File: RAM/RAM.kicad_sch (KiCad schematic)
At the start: 32 parts, among them J1 Conn_01x02_Pin, J2 Conn_01x02_Pin, J3 Conn_01x04_Pin, J4 Conn_01x04_Pin, J5 Conn_01x08_Socket, U2 CD74HCT258E, U3 SN74HCT245N, U4 CD74HCT258E, U6 CD74HCT258E

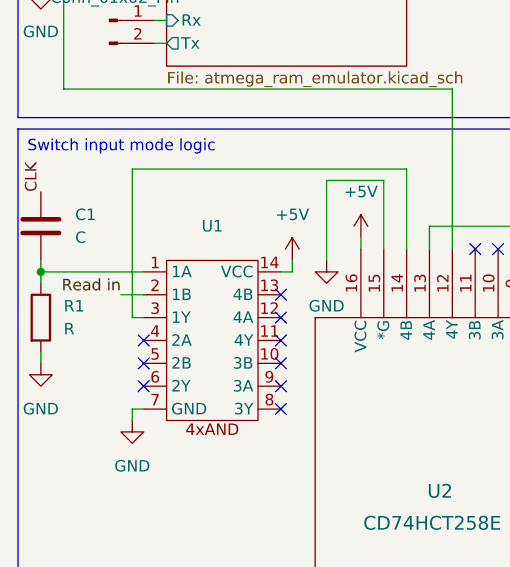
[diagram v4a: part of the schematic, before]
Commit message: Assigned footprints to all RAM components except crystal. No datasheet so waiting for delivery to hopefully get more detail or measure
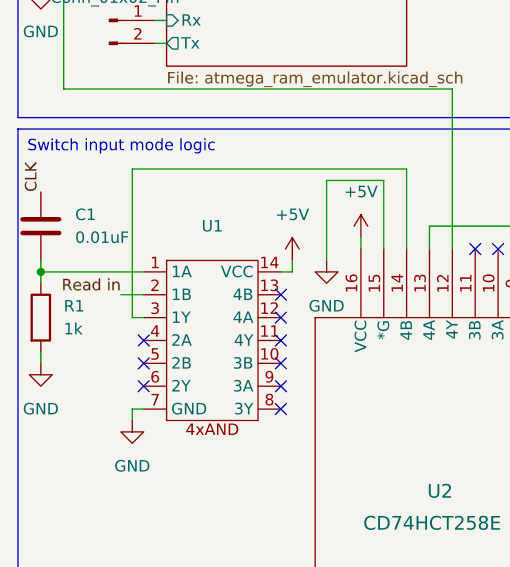
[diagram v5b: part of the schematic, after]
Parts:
- C1: value C -> 0.01uF; footprint (none) -> Capacitor_THT:C_Disc_D5.0mm_W2.5mm_P2.50mm
- J1, J2: footprint (none) -> Connector_PinHeader_1.00mm:PinHeader_1x02_P1.00mm_Vertical
- J3, J4: footprint (none) -> Connector_PinHeader_1.00mm:PinHeader_1x04_P1.00mm_Horizontal
- R1: value R -> 1k; footprint (none) -> _DownloadFootprints:CF_series_Resistors_THT
- U1: footprint (none) -> 8BitCPUFootprints:4x_and
- U2, U4, U6: footprint N16 -> _DownloadFootprints:2_to_1_selector
- U5: footprint (none) -> Package_DIP:DIP-16_W7.62mm
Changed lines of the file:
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@@
 			)
 		)
-		(property "Footprint" ""
+		(property "Footprint" "Package_DIP:DIP-16_W7.62mm"
 			(at 203.2 146.05 0)
 			(effects
@@
 			)
 		)
-		(property "Footprint" "N16"
+		(property "Footprint" "_DownloadFootprints:2_to_1_selector"
 			(at 184.15 88.9 0)
 			(effects
@@
 			)
 		)
-		(property "Footprint" ""
+		(property "Footprint" "Connector_PinHeader_1.00mm:PinHeader_1x02_P1.00mm_Vertical"
 			(at 30.48 100.33 0)
 			(effects
@@
 			)
 		)
-		(property "Footprint" ""
+		(property "Footprint" "Connector_PinHeader_1.00mm:PinHeader_1x02_P1.00mm_Vertical"
 			(at 30.48 60.96 0)
 			(effects
@@
 			)
 		)
-		(property "Footprint" "N16"
+		(property "Footprint" "_DownloadFootprints:2_to_1_selector"
 			(at 214.63 88.9 0)
 			(effects
@@
 			)
 		)
-		(property "Value" "R"
+		(property "Value" "1k"
 			(at 25.4 134.6199 0)
 			(effects
@@
 			)
 		)
-		(property "Footprint" ""
+		(property "Footprint" "_DownloadFootprints:CF_series_Resistors_THT"
 			(at 21.082 133.35 90)
 			(effects
@@
 			)
 		)
-		(property "Footprint" ""
+		(property "Footprint" "Connector_PinHeader_1.00mm:PinHeader_1x04_P1.00mm_Horizontal"
 			(at 266.7 38.1 0)
 			(effects
@@
 			)
 		)
-		(property "Footprint" "N16"
+		(property "Footprint" "_DownloadFootprints:2_to_1_selector"
 			(at 58.42 181.61 0)
 			(effects
@@
 			)
 		)
-		(property "Value" "C"
+		(property "Value" "0.01uF"
 			(at 26.67 124.4599 0)
 			(effects
@@
 			)
 		)
-		(property "Footprint" ""
+		(property "Footprint" "Capacitor_THT:C_Disc_D5.0mm_W2.5mm_P2.50mm"
 			(at 23.8252 127 0)
 			(effects
@@
 			)
 		)
-		(property "Footprint" ""
+		(property "Footprint" "Connector_PinHeader_1.00mm:PinHeader_1x04_P1.00mm_Horizontal"
 			(at 49.53 20.32 0)
 			(effects
@@
 			)
 		)
-		(property "Footprint" ""
+		(property "Footprint" "8BitCPUFootprints:4x_and"
 			(at 36.83 133.35 0)
 			(effects

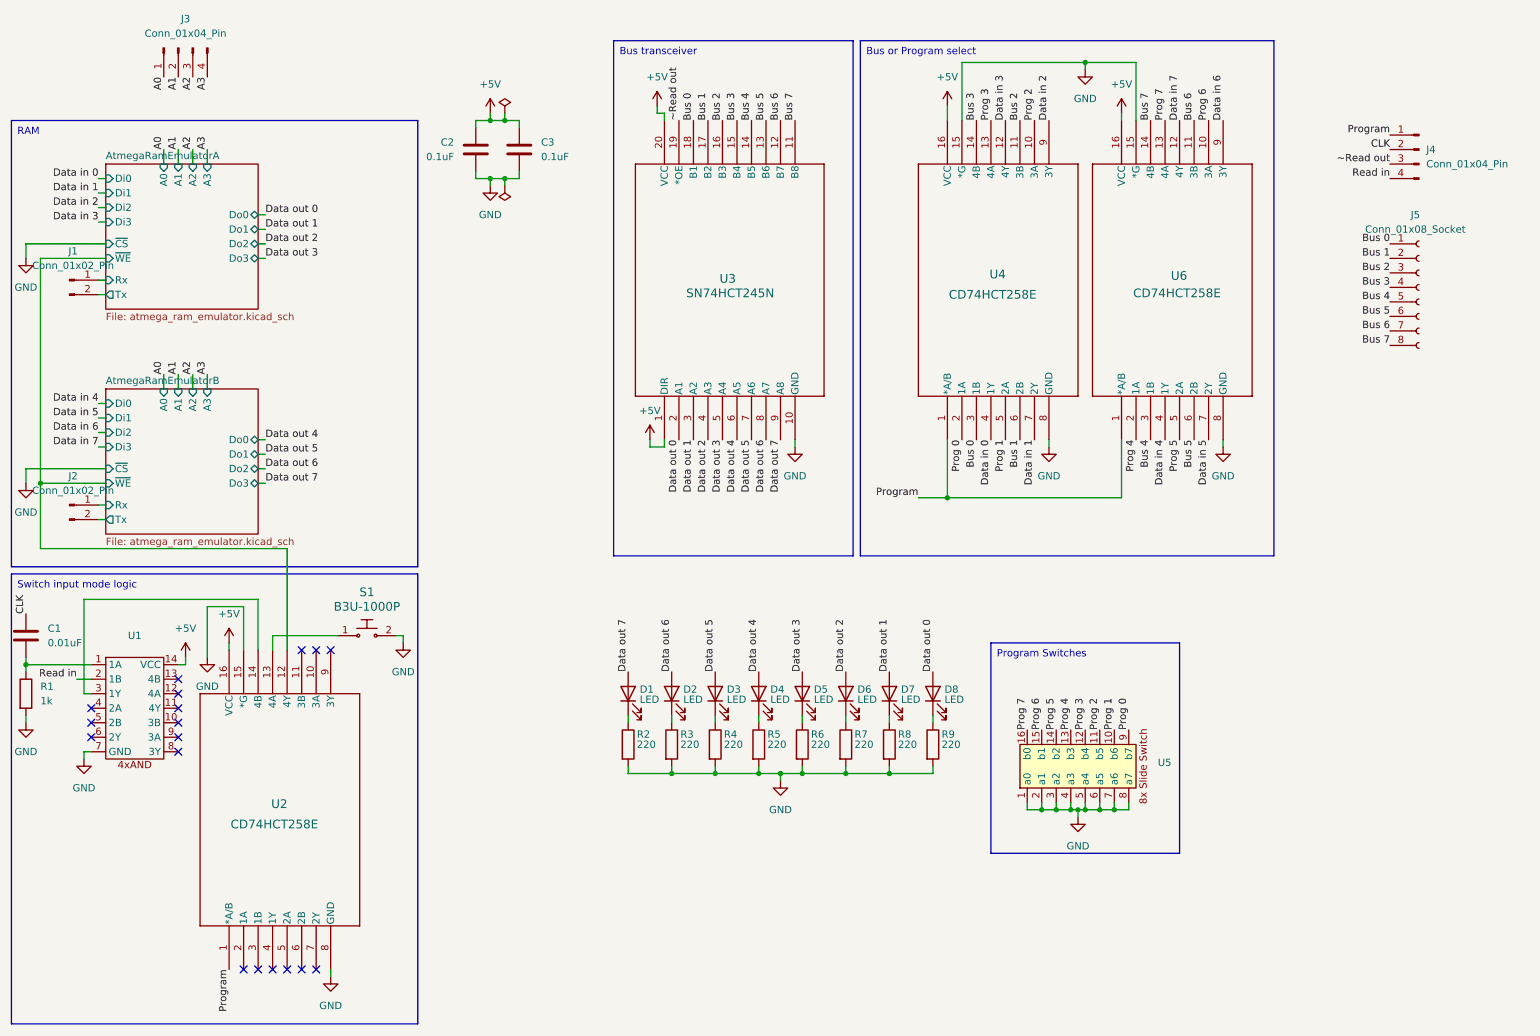
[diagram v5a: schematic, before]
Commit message: RAM module layout complete except footprint for crystal
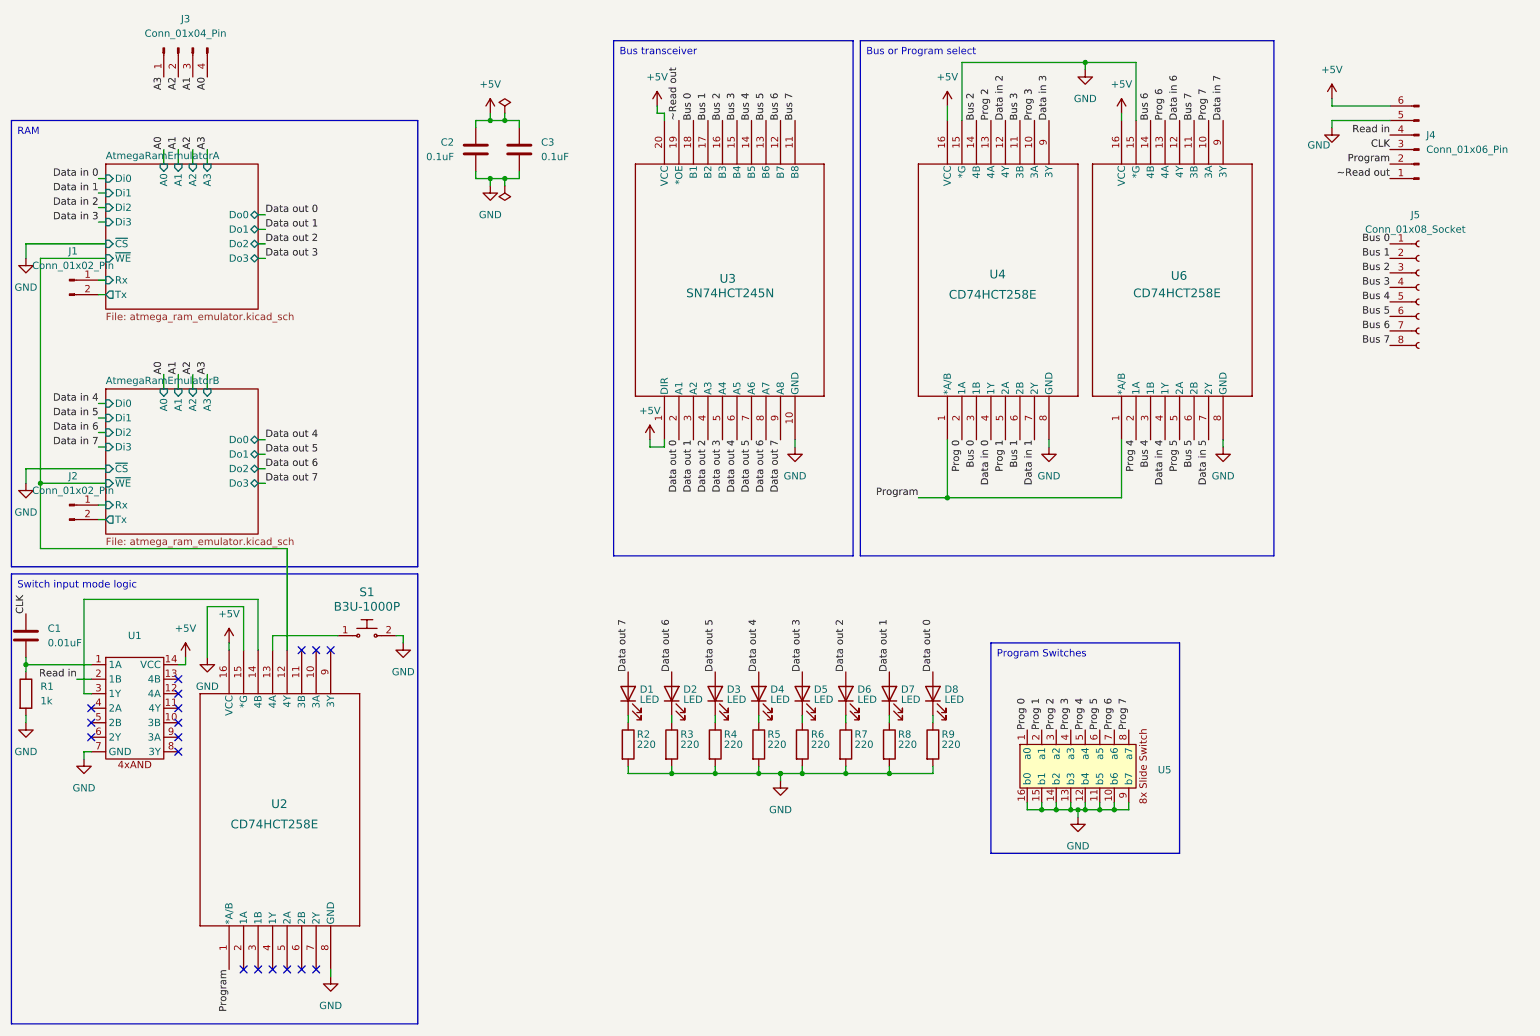
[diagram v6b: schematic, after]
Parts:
- removed J4: Conn_01x04_Pin, Connector_PinHeader_1.00mm:PinHeader_1x04_P1.00mm_Horizontal, symbol Connector:Conn_01x04_Pin
- added J4: Conn_01x06_Pin, Connector_PinHeader_1.00mm:PinHeader_1x06_P1.00mm_Horizontal, symbol Connector:Conn_01x06_Pin
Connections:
- net +5V: now also J4.6 (Pin_6)
- net A0: now also J3.4 (Pin_4); no longer J3.1 (Pin_1)
- net A1: now also J3.3 (Pin_3); no longer J3.2 (Pin_2)
- net A2: now also J3.2 (Pin_2); no longer J3.3 (Pin_3)
- net A3: now also J3.1 (Pin_1); no longer J3.4 (Pin_4)
- net Bus 2: now also U4.14 (4B); no longer U4.11 (3B)
- net Bus 3: now also U4.11 (3B); no longer U4.14 (4B)
- net Bus 6: now also U6.14 (4B); no longer U6.11 (3B)
- net Bus 7: now also U6.11 (3B); no longer U6.14 (4B)
- net CLK: now also J4.3 (Pin_3)
- net Data in 2: now also U4.12 (4Y); no longer U4.9 (3Y)
- net Data in 3: now also U4.9 (3Y); no longer U4.12 (4Y)
- net Data in 6: now also U6.12 (4Y); no longer U6.9 (3Y)
- net Data in 7: now also U6.9 (3Y); no longer U6.12 (4Y)
- net GND: now also U5.10 (b6), U5.11 (b5), U5.12 (b4), U5.13 (b3), U5.14 (b2), U5.15 (b1), U5.16 (b0), U5.9 (b7), J4.5 (Pin_5); no longer U5.1 (a0), U5.2 (a1), U5.3 (a2), U5.4 (a3), U5.5 (a4), U5.6 (a5), U5.7 (a6), U5.8 (a7)
- net Prog 0: now also U5.1 (a0); no longer U5.9 (b7)
- net Prog 1: now also U5.2 (a1); no longer U5.10 (b6)
- net Prog 2: now also U4.13 (4A), U5.3 (a2); no longer U4.10 (3A), U5.11 (b5)
- net Prog 3: now also U4.10 (3A), U5.4 (a3); no longer U4.13 (4A), U5.12 (b4)
- net Prog 4: now also U5.5 (a4); no longer U5.13 (b3)
- net Prog 5: now also U5.6 (a5); no longer U5.14 (b2)
- net Prog 6: now also U5.7 (a6), U6.13 (4A); no longer U5.15 (b1), U6.10 (3A)
- net Prog 7: now also U5.8 (a7), U6.10 (3A); no longer U5.16 (b0), U6.13 (4A)
- net Program: now also J4.2 (Pin_2)
- net Read in: now also J4.4 (Pin_4)
- net ~Read out: now also J4.1 (Pin_1)

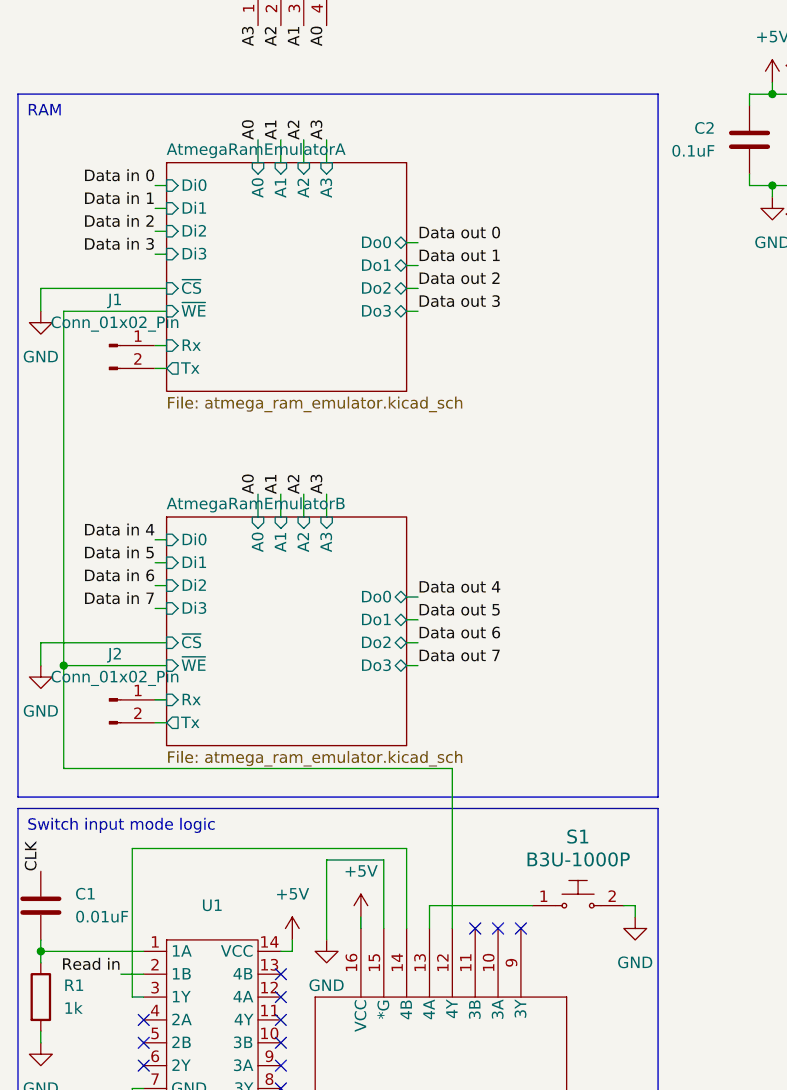
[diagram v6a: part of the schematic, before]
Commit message: Exposed SPI and RST on atmega chips
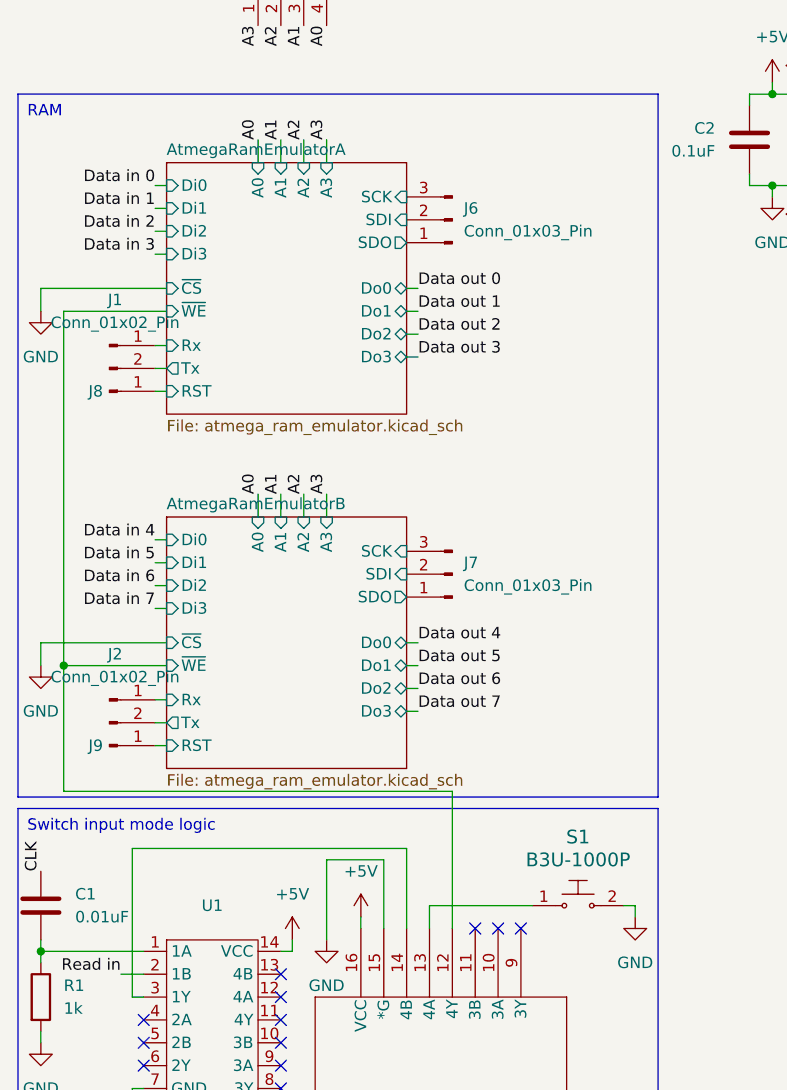
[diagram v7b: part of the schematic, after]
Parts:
- added J6, J7: Conn_01x03_Pin, Connector_PinHeader_1.00mm:PinHeader_1x03_P1.00mm_Vertical, symbol Connector:Conn_01x03_Pin
- added J8, J9: Conn_01x01_Pin, Connector_PinHeader_1.00mm:PinHeader_1x01_P1.00mm_Vertical, symbol Connector:Conn_01x01_Pin
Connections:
- new net AtmegaRamEmulatorA/RST: J8.1 (Pin_1)
- new net AtmegaRamEmulatorA/SCK: J6.3 (Pin_3)
- new net AtmegaRamEmulatorA/SDI: J6.2 (Pin_2)
- new net AtmegaRamEmulatorA/SDO: J6.1 (Pin_1)
- new net AtmegaRamEmulatorB/RST: J9.1 (Pin_1)
- new net AtmegaRamEmulatorB/SCK: J7.3 (Pin_3)
- new net AtmegaRamEmulatorB/SDI: J7.2 (Pin_2)
- new net AtmegaRamEmulatorB/SDO: J7.1 (Pin_1)
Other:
- sheet AtmegaRamEmulatorA ports: added RST, SCK, SDI, SDO; removed none
- sheet AtmegaRamEmulatorB ports: added RST, SCK, SDI, SDO; removed none

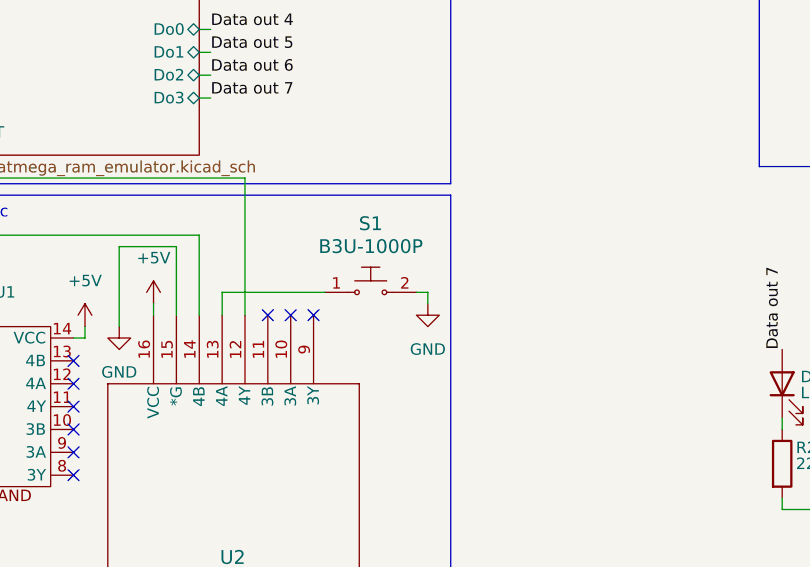
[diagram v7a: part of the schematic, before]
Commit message: Updated RAM push button to use pins that aren't shorted together
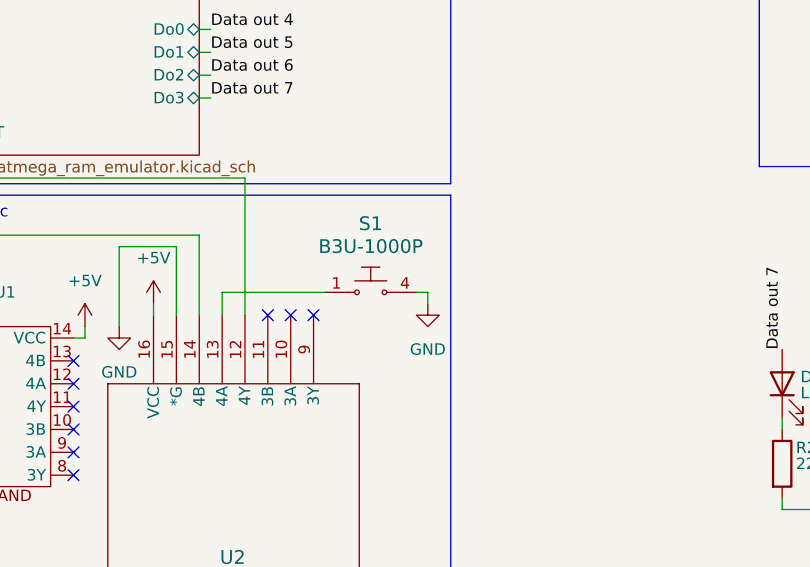
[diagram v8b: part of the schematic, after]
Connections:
- net GND: now also S1.4; no longer S1.2
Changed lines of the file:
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@@
 			)
 		)
-		(pin "2"
+		(pin "4"
 		)
 		(pin "1"
